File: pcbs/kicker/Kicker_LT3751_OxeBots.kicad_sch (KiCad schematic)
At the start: 91 parts, among them J1 XT30PW-F, J2 Conn_01x02, J3 Conn_01x02, J4 Conn_01x08, J5 XT30PW-F, Q1 BC847, Q2 BC847, Q3 IRFB4227, Q4 TIC106, Q5 FQPF20N60, T1 DCT15EFD-U44S003, U1 LM324, U2 LMV358, U3 TLV431DBZ, U4 LT3751, U5 AQV454, U6 HCNR201, U7 HCPL-3120, U8 LM358

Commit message: Desenhada versão inicial da PCB.
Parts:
- removed C6: 100nF, Capacitor_SMD:C_0805_2012Metric_Pad1.18x1.45mm_HandSolder, symbol Device:C
- removed R13, R8, R9: 10k, Resistor_SMD:R_0805_2012Metric_Pad1.20x1.40mm_HandSolder, symbol Device:R
- removed R27: 5.6k, Resistor_SMD:R_0805_2012Metric_Pad1.20x1.40mm_HandSolder, symbol Device:R
- removed R28, R5: 1k, Resistor_SMD:R_0805_2012Metric_Pad1.20x1.40mm_HandSolder, symbol Device:R
- removed U2: LMV358, Package_SO:SOIC-8_5.3x6.2mm_P1.27mm, symbol Amplifier_Operational:LM358
- C8: footprint Capacitor_THT:C_Disc_D5.0mm_W2.5mm_P2.50mm -> Capacitor_SMD:C_0805_2012Metric_Pad1.18x1.45mm_HandSolder
- R34: footprint Resistor_THT:R_Axial_DIN0207_L6.3mm_D2.5mm_P7.62mm_Horizontal -> Resistor_THT:R_Axial_DIN0207_L6.3mm_D2.5mm_P15.24mm_Horizontal
- R42: footprint Resistor_THT:R_Axial_DIN0207_L6.3mm_D2.5mm_P15.24mm_Horizontal -> Resistor_THT:R_Axial_DIN0207_L6.3mm_D2.5mm_P7.62mm_Horizontal
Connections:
- net EXT_OUT_FB: now also J4.5 (Pin_5), R12.1; no longer J4.3 (Pin_3)
- net EXT_OUT_LT3751_DONE: now also J4.4 (Pin_4); no longer J4.5 (Pin_5)
- net EXT_OUT_LT3751_FAULT: now also J4.3 (Pin_3); no longer J4.4 (Pin_4)
- net GND: now also U1.12 (+); no longer U1.10 (+)
- net GNDPWR: now also U8.5 (+); no longer U8.3 (+)
- net at R44.2, R45.1: now also U8.3 (+); no longer U8.5 (+)
- net at C9.2, RV2.2, RV2.3: now also U1.10 (+), U1.14; no longer U1.5 (+), U1.8
- net at C9.1, R31.2, U6.6: now also U1.13 (-); no longer U1.9 (-)
- net at U1.1, U1.2 (-): now also R12.2; no longer R14.2
- net at R23.2, RV1.1: now also U1.5 (+); no longer U1.3 (+)
- net at R36.2: now also U8.7; no longer U8.1
- net at R41.1, U6.3: now also U8.6 (-); no longer U8.2 (-)
- net at R23.1, R25.1: now also U1.8, U1.9 (-); no longer U1.6 (-), U1.7
- net at R25.2, R26.1: now also U1.3 (+); no longer U1.12 (+)
- new net: R41.2, U8.1, U8.2 (-)
- new net: R14.2, U1.6 (-), U1.7
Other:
- moved on the sheet: U1A, U1B, U1C, U1D, U8A, U8B

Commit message: Revisados os furos e adicionado MCU STM32
* Adicionado MCU STM32
* Corrigida posição dos furos
* Invertida a posição dos capacitores
* Realizadas melhorias na em geral
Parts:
- removed D1: MUR460, Diode_THT:D_DO-201AD_P12.70mm_Horizontal, symbol Device:D
- removed D2: 1N4712A, Diode_THT:D_DO-41_SOD81_P7.62mm_Horizontal, symbol Diode:1N47xxA
- removed D3: 1.5KE220A, Diode_THT:D_DO-201AE_P15.24mm_Horizontal, symbol Diode:1.5KExxA
- removed J4: Conn_01x08, Connector_PinHeader_2.54mm:PinHeader_1x08_P2.54mm_Vertical, symbol Connector_Generic:Conn_01x08
- removed PS1: B1215S, Converter_DCDC:Converter_DCDC_Murata_MEE1SxxxxSC_THT, symbol Converter_DCDC:MEE1S1515SC
- removed Q4: TIC106, Package_TO_SOT_THT:TO-220-3_Vertical, symbol Triac_Thyristor:TIC106
- removed R10: 1.2k, Resistor_SMD:R_0805_2012Metric_Pad1.20x1.40mm_HandSolder, symbol Device:R
- removed R11: 9.1k, Resistor_SMD:R_0805_2012Metric_Pad1.20x1.40mm_HandSolder, symbol Device:R
- removed R12: 10k, Resistor_SMD:R_0805_2012Metric_Pad1.20x1.40mm_HandSolder, symbol Device:R
- removed R14: 1k, Resistor_SMD:R_0805_2012Metric_Pad1.20x1.40mm_HandSolder, symbol Device:R
- removed R34: 27k, Resistor_THT:R_Axial_DIN0207_L6.3mm_D2.5mm_P15.24mm_Horizontal, symbol Device:R
- removed R35: 18k, Resistor_THT:R_Axial_DIN0207_L6.3mm_D2.5mm_P7.62mm_Horizontal, symbol Device:R
- removed RV1: 100k, Potentiometer_THT:Potentiometer_Bourns_3296W_Vertical, symbol Device:R_Potentiometer_Trim
- removed U1: LM324, Package_SO:SOIC-14_3.9x8.7mm_P1.27mm, symbol Amplifier_Operational:LM324
- removed U3: TLV431DBZ, Package_TO_SOT_SMD:SOT-23, symbol Reference_Voltage:TL431DBZ
- added C17, C20: 100nF, Capacitor_SMD:C_0805_2012Metric_Pad1.18x1.45mm_HandSolder, symbol Device:C
- added D2, D3: MURS460, Diode_SMD:D_SMC_Handsoldering, symbol Device:D
- added D4: LED, LED_THT:LED_D5.0mm, symbol Device:LED
- added D5: LED, LED_THT:LED_D3.0mm, symbol Device:LED
- added H1, H2: MountingHole, MountingHole:MountingHole_4.3mm_M4_Pad_Via, symbol Mechanical:MountingHole
- added J5: I2C, Connector_JST:JST_PH_S4B-PH-K_1x04_P2.00mm_Horizontal, symbol Connector_Generic:Conn_01x04
- added J6: ST Link, Connector_PinHeader_2.54mm:PinHeader_1x04_P2.54mm_Horizontal, symbol Connector_Generic:Conn_01x04
- added JP1: Boot0, Connector_PinHeader_2.54mm:PinHeader_1x03_P2.54mm_Horizontal, symbol Jumper:Jumper_3_Open
- added PS1: B1215S, oxebots:DC-DC_Converter_BxxxxS_1W, symbol oxebots:Converter_DC-DC_BxxxxS
- added Q5, Q6: BSS138, Package_TO_SOT_SMD:SOT-23, symbol Transistor_FET:BSS138
- added R22: 12k 2W, Resistor_SMD:R_2512_6332Metric_Pad1.40x3.35mm_HandSolder, symbol Device:R
- added R27: 10R, Resistor_SMD:R_0805_2012Metric_Pad1.20x1.40mm_HandSolder, symbol Device:R
- added R28, R32, R38, R39: 10k, Resistor_SMD:R_0805_2012Metric_Pad1.20x1.40mm_HandSolder, symbol Device:R
- added SW1: SW_Push, Button_Switch_SMD:SW_SPST_SKQG_WithStem, symbol Switch:SW_Push
- added TP1: +24V, TestPoint:TestPoint_Pad_D1.5mm, symbol Connector:TestPoint
- added TP10: SOL+, TestPoint:TestPoint_Pad_D1.5mm, symbol Connector:TestPoint
- added TP11: KICK_PWM, TestPoint:TestPoint_Pad_D1.5mm, symbol Connector:TestPoint
- added TP12: SOL-, TestPoint:TestPoint_Pad_D1.5mm, symbol Connector:TestPoint
- added TP13: FAULT, TestPoint:TestPoint_Pad_D1.5mm, symbol Connector:TestPoint
- added TP14: BLEEDER, TestPoint:TestPoint_Pad_D1.5mm, symbol Connector:TestPoint
- added TP15: VD_SEC, TestPoint:TestPoint_Pad_D1.5mm, symbol Connector:TestPoint
- added TP16: VD_SEC_BUFFER, TestPoint:TestPoint_Pad_D1.5mm, symbol Connector:TestPoint
- added TP17, TP19: FB_ANALOG, TestPoint:TestPoint_Pad_D1.5mm, symbol Connector:TestPoint
- added TP18: FB_PWM, TestPoint:TestPoint_Pad_D1.5mm, symbol Connector:TestPoint
- added TP2: VCAP, TestPoint:TestPoint_Pad_D1.5mm, symbol Connector:TestPoint
- added TP3: +12V, TestPoint:TestPoint_Pad_D1.5mm, symbol Connector:TestPoint
- added TP4: HVGATE, TestPoint:TestPoint_Pad_D1.5mm, symbol Connector:TestPoint
- added TP5: CSP, TestPoint:TestPoint_Pad_D1.5mm, symbol Connector:TestPoint
- added TP6: +3.3V, TestPoint:TestPoint_Pad_D1.5mm, symbol Connector:TestPoint
- added TP7: GND, TestPoint:TestPoint_Pad_D1.5mm, symbol Connector:TestPoint
- added TP8: +15V_SEC, TestPoint:TestPoint_Pad_D1.5mm, symbol Connector:TestPoint
- added TP9: DONE, TestPoint:TestPoint_Pad_D1.5mm, symbol Connector:TestPoint
- added U4: STM32F070F6Px, Package_SO:TSSOP-20_4.4x6.5mm_P0.65mm, symbol MCU_ST_STM32F0:STM32F070F6Px
- added U7: TLV9002, Package_SO:SOIC-8_3.9x4.9mm_P1.27mm, symbol oxebots:TLV9002
- C11: renamed from C10; footprint Capacitor_THT:C_Disc_D5.0mm_W2.5mm_P2.50mm -> Capacitor_SMD:C_0805_2012Metric_Pad1.18x1.45mm_HandSolder
- C15: footprint Capacitor_THT:C_Disc_D5.0mm_W2.5mm_P2.50mm -> Capacitor_SMD:C_0805_2012Metric_Pad1.18x1.45mm_HandSolder
- C2: renamed from C4; footprint Capacitor_THT:C_Disc_D5.0mm_W2.5mm_P2.50mm -> Capacitor_SMD:C_0805_2012Metric_Pad1.18x1.45mm_HandSolder
- C4: renamed from C11; value 22nF -> 2.2nF; footprint Capacitor_THT:C_Rect_L7.0mm_W4.5mm_P5.00mm -> Capacitor_THT:C_Rect_L10.3mm_W5.0mm_P7.50mm_MKS4
- C5: renamed from C12; footprint Capacitor_THT:C_Rect_L19.0mm_W6.0mm_P15.00mm_MKS4 -> Capacitor_THT:C_Rect_L13.0mm_W5.0mm_P10.00mm_FKS3_FKP3_MKS4
- F1: value Fuse -> 10A
- J1: footprint oxebots_connectors:AMASS_XT30PW-M -> oxebots:AMASS_XT30PW-M
- J2: renamed from J3; value Conn_01x02 -> 12V; footprint Connector_JST:JST_XH_B2B-XH-A_1x02_P2.50mm_Vertical -> Connector_JST:JST_PH_S2B-PH-K_1x02_P2.00mm_Horizontal
- J3: renamed from J2; value Conn_01x02 -> 3.3V; footprint Connector_JST:JST_XH_B2B-XH-A_1x02_P2.50mm_Vertical -> Connector_JST:JST_PH_S2B-PH-K_1x02_P2.00mm_Horizontal
- J4: renamed from J5; footprint oxebots_connectors:AMASS_XT30PW-M -> oxebots:AMASS_XT30PW-M
- Q1: renamed from Q3; footprint Package_TO_SOT_THT:TO-220-3_Vertical -> Package_TO_SOT_THT:TO-220-3_Horizontal_TabDown
- Q3: renamed from Q5; footprint Package_TO_SOT_THT:TO-220F-3_Vertical -> Package_TO_SOT_THT:TO-220-3_Horizontal_TabDown
- R1: renamed from R30; footprint Resistor_THT:R_Axial_DIN0922_L20.0mm_D9.0mm_P7.62mm_Vertical -> Resistor_THT:R_Axial_DIN0617_L17.0mm_D6.0mm_P20.32mm_Horizontal
- R10: renamed from R21; value 4.7k -> 1k
- R14: renamed from R17; value 4.7k -> 10k
- R15: renamed from R22; value 4.7k -> 1k
- R16: renamed from R33; value 220R -> 150R
- R20: renamed from R32; value 1k -> 2.7k
- R21: renamed from R39; value 1k -> 2.7k 25W
- R23: value 1k -> 12k 2W; footprint Resistor_SMD:R_0805_2012Metric_Pad1.20x1.40mm_HandSolder -> Resistor_SMD:R_2512_6332Metric_Pad1.40x3.35mm_HandSolder
- R24: value 330R -> 10R
- R25: value 20k -> 10k
- R26: value 10k -> 150R
- R29: renamed from R42; value 510k -> 330k; footprint Resistor_THT:R_Axial_DIN0207_L6.3mm_D2.5mm_P7.62mm_Horizontal -> Resistor_SMD:R_0805_2012Metric_Pad1.20x1.40mm_HandSolder
- R30: renamed from R43; value 510k -> 330k; footprint Resistor_THT:R_Axial_DIN0207_L6.3mm_D2.5mm_P7.62mm_Horizontal -> Resistor_SMD:R_0805_2012Metric_Pad1.20x1.40mm_HandSolder
- R31: renamed from R44; value 47k -> 330k; footprint Resistor_THT:R_Axial_DIN0207_L6.3mm_D2.5mm_P7.62mm_Horizontal -> Resistor_SMD:R_0805_2012Metric_Pad1.20x1.40mm_HandSolder
- R33: renamed from R31; value 270k -> 47k
- R35: renamed from R41; value 330k -> 56k
- R36: renamed from R45; value 33k -> 10k; footprint Resistor_THT:R_Axial_DIN0207_L6.3mm_D2.5mm_P7.62mm_Horizontal -> Resistor_SMD:R_0805_2012Metric_Pad1.20x1.40mm_HandSolder
- R37: value 100k -> 1k; footprint Resistor_THT:R_Axial_DIN0207_L6.3mm_D2.5mm_P7.62mm_Horizontal -> Resistor_SMD:R_0805_2012Metric_Pad1.20x1.40mm_HandSolder
- R7: value 220R -> 1k
- R8: renamed from R15; value 1,5K -> 1,8K
- R9: renamed from R16; value 4.7k -> 10k
- RV1: renamed from RV2; value 100k -> 20k; footprint Potentiometer_THT:Potentiometer_Bourns_3296W_Vertical -> oxebots:trimpot_3362P
- T1: footprint oxebots_transformer:TRANS_U44S003_TDK -> oxebots:TRANS_U44S003_TDK
- U3: renamed from U5; footprint Package_DIP:DIP-6_W7.62mm_LongPads -> Package_DIP:DIP-6_W8.89mm_SMDSocket_LongPads
- U5: renamed from U8; footprint Package_SO:SOIC-8_5.3x6.2mm_P1.27mm -> Package_SO:SOIC-8_3.9x4.9mm_P1.27mm
- renumbered C2 to C10, C14 to C12, C17 to C13, C13 to C14, C9 to C16, C5 to C18, C7 to C3, C16 to C6, C18 to C7, C3 to C8, C8 to C9, D4 to D1, Q1 to Q2, Q2 to Q4, R1 to R11, R2 to R12, R3 to R13, R38 to R17, R4 to R18, R40 to R19, R18 to R2, R19 to R3, R36 to R34, R6 to R4, R20 to R5, R29 to R6, U4 to U1, U7 to U2
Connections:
- net +12V: now also R24.1, PS1.2 (+Vin), TP3.1; no longer C18.1, R20.1
- net +15V_SEC: now also PS1.4 (+Vout), TP8.1
- net +24V: now also R20.1, TP1.1
- net +3.3V: now also C15.1, C18.1, R26.1, J5.4 (Pin_4), J6.1 (Pin_1), JP1.1 (A), R32.1, TP6.1, U4.16 (VDD), U4.5 (VDDA), U7.8 (V+)
- net GND: now also C15.2, R25.2, C17.2, C20.2, D5.1 (K), J5.1 (Pin_1), J6.4 (Pin_4), JP1.3 (B), PS1.1 (-Vin), Q6.2 (S), R28.2, SW1.1, TP7.1, U4.15 (VSS), U7.3 (+), U7.4 (V-); no longer R24.2, R26.2, U3.2
- net GNDPWR: now also U3.4, PS1.3 (-Vout); no longer C15.2, R37.2
- net LT3751_FB: now also C20.1, R38.2, TP19.1
- net VCAP: now also R21.2, R23.2, D2.1 (K), D3.1 (K), TP10.1, TP2.1; no longer R21.1
- net at R31.2, R36.1, U5.3 (+): now also TP15.1
- net at C16.2, RV1.2, RV1.3: now also U7.1, U7.5 (+)
- net at R25.1: now also R24.2, Q5.1 (G); no longer R23.1
- net at C16.1, R33.2, U6.6: now also U7.2 (-)
- net at R35.2, U5.1, U5.2 (-): now also TP16.1
- net MCU_ADC_IN_FB: now reaches R37.1
- net MCU_ADC_IN_FB: now also TP17.1, U4.6 (PA0); no longer C15.1
- net at J4.N, Q3.2 (D): now also D3.2 (A), TP12.1
- net at R17.1, U2.7 (VO): no longer U2.6 (VO)
- net at U3.6: now also R21.1, D4.1 (K)
- net at Q1.1 (G), R5.2: now also TP4.1
- net at Q1.3 (S), R6.1, U1.12 (CSP): now also TP5.1
- net at T1.1: now also D2.2 (A)
- net EXT_IN_LT3751_ENABLE renamed MCU_OUT_ENABLE
- net MCU_OUT_ENABLE: now also U4.11 (PA5)
- net EXT_IN_LT3751_KICK_1 renamed MCU_PWM_OUT_KICK
- net MCU_PWM_OUT_KICK: now also TP11.1, U4.10 (PA4)
- net EXT_OUT_LT3751_DONE renamed MCU_IN_DONE
- net MCU_IN_DONE: now also TP9.1, U4.13 (PA7)
- net EXT_OUT_LT3751_FAULT renamed MCU_IN_FAULT
- net MCU_IN_FAULT: now also TP13.1, U4.14 (PB1)
- new net: Q5.2 (S), Q6.3 (D)
- new net: Q5.3 (D), U3.2
- new net: JP1.2 (C), R39.1
- new net: R37.2, U7.6 (-), U7.7
- new net: Q6.1 (G), R27.2, R28.1
- new net: D5.2 (A), R26.2
- new net: D4.2 (A), R22.1
- new net: R22.2, R23.1
- new net MCU_BOOT0: R39.2, U4.1 (BOOT0)
- new net MCU_I2C_SCL: J5.3 (Pin_3), U4.17 (PA9/PA11)
- new net MCU_I2C_SDA: J5.2 (Pin_2), U4.18 (PA10/PA12)
- new net MCU_NRST: C17.1, R32.2, SW1.2, U4.4 (NRST)
- new net MCU_OUT_BLEEDER: R27.1, TP14.1, U4.9 (PA3)
- new net MCU_PWM_OUT_FB: R38.1, TP18.1, U4.12 (PA6)
- new net MCU_STLINK_SWCLK: J6.3 (Pin_3), U4.20 (PA14)
- new net MCU_STLINK_SWDIO: J6.2 (Pin_2), U4.19 (PA13)
- no-connect marks 4 -> 9
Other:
- note added: "BOOT0"
- note added: "External Interface I2C"
- note added: "External Interface ST Link"
- note added: "Feedback PWM to Analog Low-Pass Filter"
- note added: "Isolated Power +15V"
- note added: "Microcontroller"
- note added: "Mounting Holes"
- note added: "Reset Switch"
- note removed: "50W Com dissipador"
- note removed: "5W"
- note removed: "External Interfaces"
- note removed: "Isolated Power +5V e +15V"
- moved on the sheet: C1, C10, C11, C12, C13, C14, C16, C18, C19, C2, C3, C4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

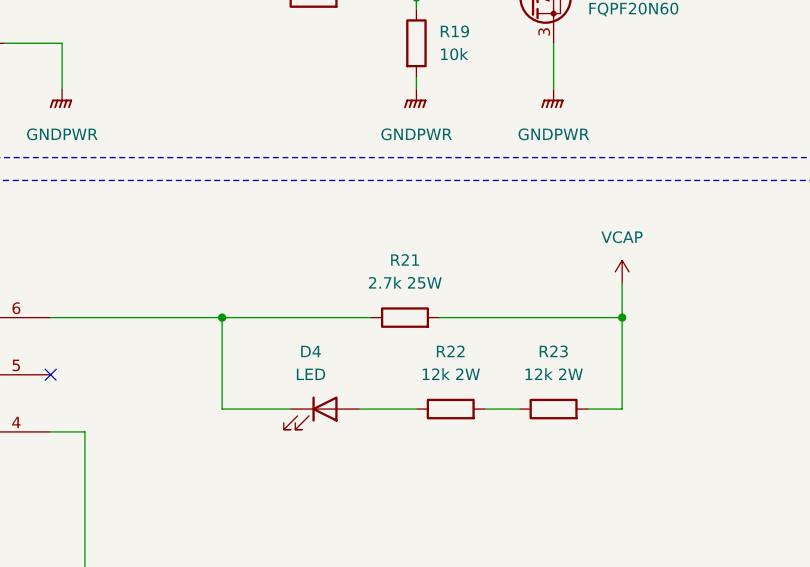
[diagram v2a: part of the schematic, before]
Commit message: Ajustes no resistor do led do AQV454
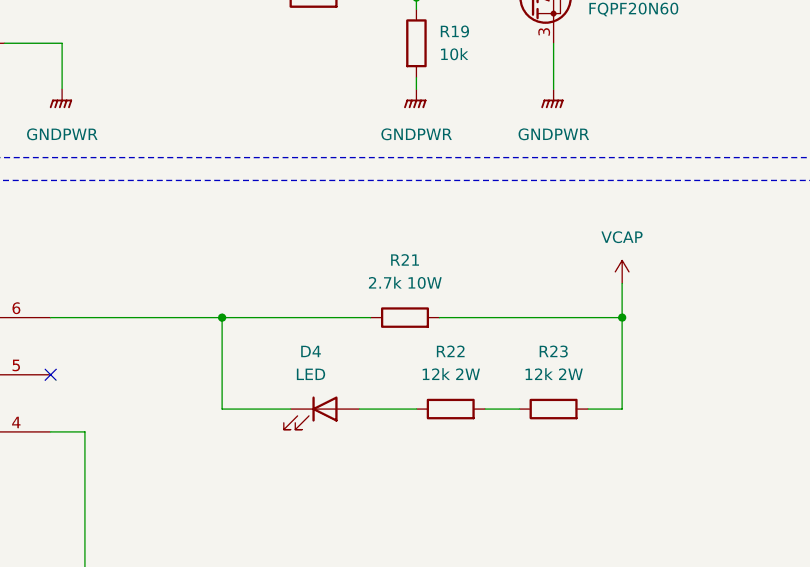
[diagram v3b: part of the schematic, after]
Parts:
- R20: footprint Resistor_SMD:R_0805_2012Metric_Pad1.20x1.40mm_HandSolder -> Resistor_SMD:R_2512_6332Metric_Pad1.40x3.35mm_HandSolder
- R21: value 2.7k 25W -> 2.7k 10W

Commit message: Replaced MCU
Replaced MCU STM32F070F6P6 with STM32G031F6P6
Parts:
- removed C13: 220uF, Capacitor_THT:CP_Radial_D8.0mm_P5.00mm, symbol Device:C_US
- removed JP1: Boot0, Connector_PinHeader_2.54mm:PinHeader_1x03_P2.54mm_Horizontal, symbol Jumper:Jumper_3_Open
- removed PS1: B1215S, oxebots:DC-DC_Converter_BxxxxS_1W, symbol oxebots:Converter_DC-DC_BxxxxS
- removed Q2, Q4: BC847, Package_TO_SOT_SMD:SOT-23, symbol Transistor_BJT:BC847
- removed R10, R15: 1k, Resistor_SMD:R_0805_2012Metric_Pad1.20x1.40mm_HandSolder, symbol Device:R
- removed R39: 10k, Resistor_SMD:R_0805_2012Metric_Pad1.20x1.40mm_HandSolder, symbol Device:R
- removed U4: STM32F070F6Px, Package_SO:TSSOP-20_4.4x6.5mm_P0.65mm, symbol MCU_ST_STM32F0:STM32F070F6Px
- added C10, C24: 100nF, Capacitor_SMD:C_0805_2012Metric_Pad1.18x1.45mm_HandSolder, symbol Device:C
- added C11, C12, C13, C14, C15, C16, C17: 1nF, Capacitor_SMD:C_0805_2012Metric_Pad1.18x1.45mm_HandSolder, symbol Device:C
- added C28, C5: 470uF, Capacitor_SMD:CP_Elec_8x10, symbol Device:C_US
- added C9: 10uF, Capacitor_SMD:C_0805_2012Metric_Pad1.18x1.45mm_HandSolder, symbol Device:C
- added JP1: UVLO1_BYPASS, Jumper:SolderJumper-2_P1.3mm_Open_RoundedPad1.0x1.5mm, symbol Jumper:Jumper_2_Open
- added JP2: OVLO1_BYPASS, Jumper:SolderJumper-2_P1.3mm_Open_RoundedPad1.0x1.5mm, symbol Jumper:Jumper_2_Open
- added JP3: UVLO2_BYPASS, Jumper:SolderJumper-2_P1.3mm_Open_RoundedPad1.0x1.5mm, symbol Jumper:Jumper_2_Open
- added JP4: OVLO2_BYPASS, Jumper:SolderJumper-2_P1.3mm_Open_RoundedPad1.0x1.5mm, symbol Jumper:Jumper_2_Open
- added NT1: NetTie_2, NetTie:NetTie-2_SMD_Pad0.5mm, symbol Device:NetTie_2
- added PS1: Converter_DC-DC_BxxxxS 1W, oxebots:DC-DC_Converter_BxxxxS_1W, symbol oxebots:Converter_DC-DC_BxxxxS_1W
- added R7: 10k, Resistor_SMD:R_0805_2012Metric_Pad1.20x1.40mm_HandSolder, symbol Device:R
- added U1: STM32G031F6Px, Package_SO:TSSOP-20_4.4x6.5mm_P0.65mm, symbol MCU_ST_STM32G0:STM32G031F6Px
- C1: value 1000uF -> 470uF; footprint Capacitor_THT:CP_Radial_D8.0mm_P5.00mm -> Capacitor_SMD:CP_Elec_10x12.5
- C26: renamed from C12; footprint Capacitor_THT:C_Disc_D5.0mm_W2.5mm_P2.50mm -> Capacitor_SMD:C_0805_2012Metric_Pad1.18x1.45mm_HandSolder
- C7: renamed from C3; value 100nF -> 10uF
- F1: footprint Fuse:Fuse_Blade_ATO_directSolder -> Fuse:Fuse_Blade_Mini_directSolder
- R11: renamed from R8; value 1,8K -> 1,8K (NOTA 3)
- R12: renamed from R14; value 10k -> 100k
- R13: renamed from R38; value 10k -> 4.7k
- R17: renamed from R6; value 25m (NOTA 1) -> 25m (NOTA 2)
- R23: renamed from R1; value 4,7K -> 47R 5W
- R25: renamed from R33; value 47k -> 51k
- R5: renamed from R9; value 10k -> 100k
- RV1: value 20k -> 10k
- U2: renamed from U1; footprint Package_SO:TSSOP-20-1EP_4.4x6.5mm_P0.65mm_EP2.15x3.35mm -> oxebots:LT3751
- U4: renamed from U3; footprint Package_DIP:DIP-6_W8.89mm_SMDSocket_LongPads -> oxebots:AQV454; symbol oxebots:AQV453 -> oxebots:AQV454
- renumbered C20 to C18, C9 to C19, C10 to C2, C18 to C20, C16 to C21, C11 to C22, C4 to C23, C5 to C25, C14 to C27, C19 to C29, C8 to C3, C6 to C30, C7 to C31, C2 to C4, C15 to C6, C17 to C8, D5 to D1, D1 to D2, D2 to D3, D3 to D5, J5 to J4, J6 to J5, J4 to J6, Q5 to Q2, Q6 to Q3, Q3 to Q4, R26 to R1, R18 to R10, R2 to R14, R3 to R15, R5 to R16, R37 to R18, R24 to R19, R32 to R2, R27 to R20, R25 to R21, R28 to R22, R20 to R24, R16 to R26, R34 to R27, R17 to R28, R21 to R29, R11 to R3, R35 to R30, R19 to R31, R22 to R32, R23 to R33, R29 to R34, R30 to R35, R31 to R36, R36 to R37, R12 to R4, R7 to R6, R4 to R8, R13 to R9, TP7 to TP1, TP5 to TP10, TP17 to TP11, TP14 to TP12, TP11 to TP13, TP8 to TP14, TP2 to TP15, TP10 to TP17, TP12 to TP18, TP15 to TP19, TP6 to TP2, TP1 to TP4, TP9 to TP5, TP18 to TP6, TP13 to TP7, TP19 to TP8, TP4 to TP9, U7 to U3, U6 to U5, U2 to U6, U5 to U7
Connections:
- net MCU_IN_DONE is gone; now on net LT3751_DONE: TP5.1
- net MCU_IN_FAULT is gone; now on net LT3751_FAULT: TP7.1
- net +12V: now also C10.1, C5.1, JP1.1 (A), JP3.1 (A), PS1.2 (+Vin)
- net +15V_SEC: now also C24.1, C28.1, PS1.4 (+Vout)
- net +3.3V: now also C9.1, U1.4 (VDD)
- net GND: now also C10.2, C11.2, C12.2, C13.2, C14.2, C15.2, C16.2, C17.2, C5.2, C9.2, JP2.2 (B), JP4.2 (B), NT1.2, PS1.1 (-Vin), R7.2, U1.5 (VSS); no longer U2.11 (CSN)
- net GNDPWR: now also C24.2, C28.2, PS1.3 (-Vout)
- net LT3751_DONE: now also C13.1, U1.13 (PA6)
- net LT3751_FAULT: now also C17.1, U1.14 (PA7)
- net LT3751_OVLO_1: now also C12.1, JP2.1 (A)
- net LT3751_OVLO_2: now also C16.1, JP4.1 (A)
- net LT3751_UVLO_1: now also C11.1, JP1.2 (B)
- net LT3751_UVLO_2: now also C15.1, JP3.2 (B)
- net MCU_ADC_IN_FB: now also U1.10 (PA3)
- net MCU_I2C_SCL: now also U1.20 (PB3/PB4/PB5/PB6)
- net MCU_I2C_SDA: now also U1.1 (PB7/PB8)
- net MCU_NRST: now also U1.6 (PF2)
- net MCU_OUT_BLEEDER: now also U1.7 (PA0)
- net MCU_OUT_ENABLE: now also U1.12 (PA5)
- net MCU_PWM_OUT_FB: now also U1.11 (PA4)
- net MCU_PWM_OUT_KICK: now also U1.8 (PA1)
- net MCU_STLINK_SWCLK: now also U1.19 (PA14/PA15)
- net MCU_STLINK_SWDIO: now also U1.18 (PA13)
- net at R6.2, U2.8 (CHARGE): now also C14.1, R7.1
- new net: NT1.1, U2.11 (CSN)
- no-connect marks 9 -> 11
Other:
- note added: "Power LED"
- note added: "Solenoid Connector"
- note added: "Voltage Divider 100:1"
- note removed: "BOOT0"
- moved on the sheet: C19, C23, C26, C3, C6, C8, R10, R12, R2, R23, R3, R37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
